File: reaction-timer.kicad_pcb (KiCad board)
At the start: 2 copper layers, 48 x 80 mm, 38 parts, among them IC1 4026, IC2 4026, IC3 4026, IC5 NE555P, IC6 NE555P, IC7 NE555P

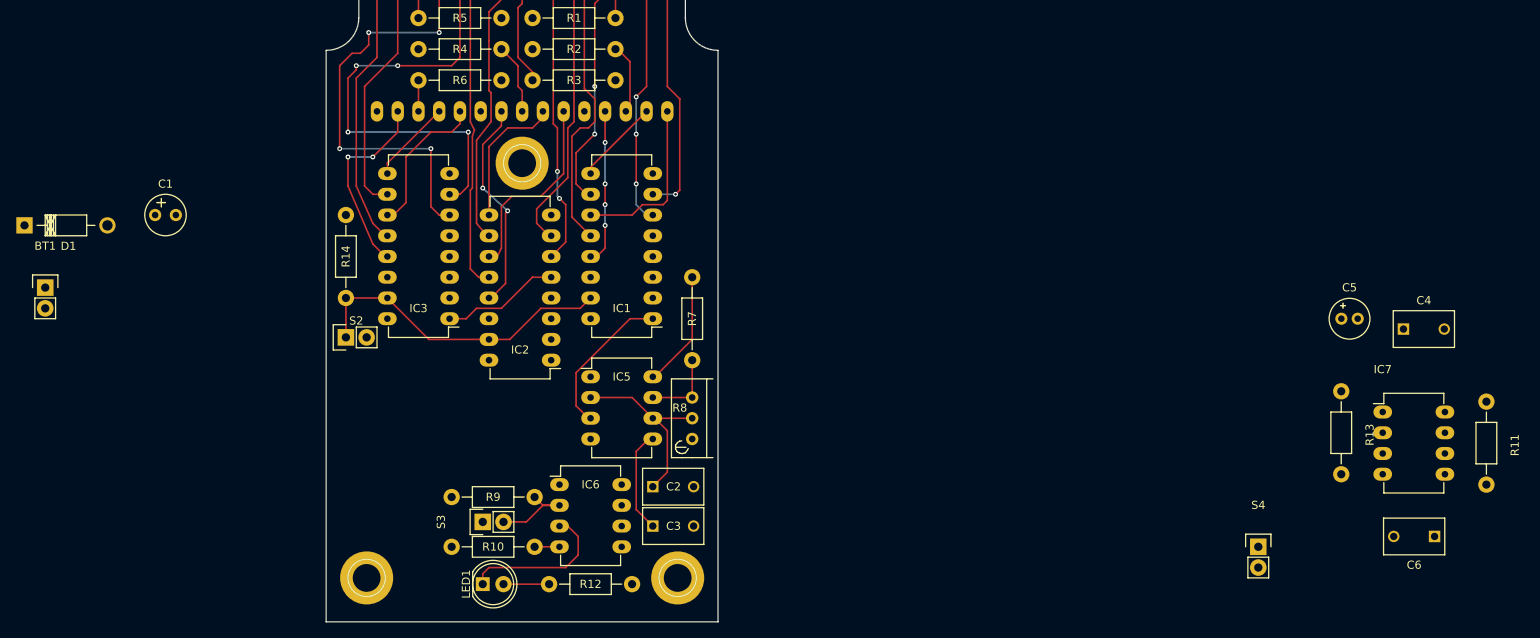
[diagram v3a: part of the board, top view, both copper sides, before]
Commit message: Place IC7
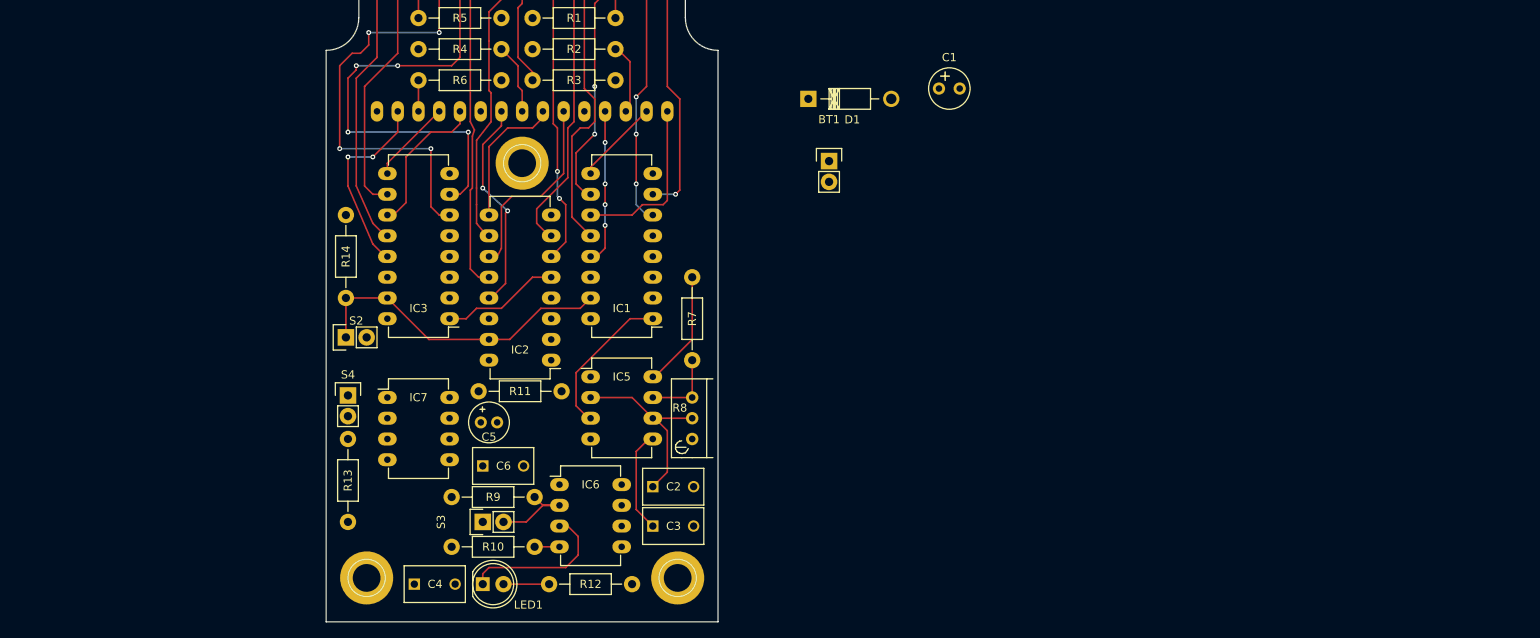
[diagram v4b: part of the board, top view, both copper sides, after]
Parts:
- moved C4 125.1 mm to (68.1, 136.7)
- moved IC7 121.9 mm to (64.8, 113.8)
- moved R13 121.8 mm to (59.9, 124.0)
- moved R11 118.5 mm to (81.0, 113.0), turned to 180 degrees
- moved C6 116.9 mm to (76.5, 122.2), turned to 0 degrees
- moved S4 113.0 mm to (59.9, 113.5)
- moved C5 106.2 mm to (76.2, 116.8)
- moved BT1 97.3 mm to (118.9, 84.8)
- moved C1 97.3 mm to (132.3, 75.9)
- moved D1 97.3 mm to (116.3, 77.2)
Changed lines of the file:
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@@
   )
   (module Pin_Headers:Pin_Header_Straight_1x02 (layer F.Cu)
-    (at 22.86 100.33)
+    (at 118.872 84.836)
     (descr "Through hole pin header")
     (tags "pin header")
@@
   )
   (module Capacitors_Elko_ThroughHole:Elko_vert_11x5mm_RM2.5 (layer F.Cu)
-    (at 36.322 91.44)
+    (at 132.334 75.946)
     (descr "Electrolytic Capacitor, vertical, diameter 5mm, radial, RM 2,5mm")
     (tags "Electrolytic Capacitor, vertical, diameter 5mm, radial, RM 2,5mm, Elko, Electrolytkondensator, Kondensator gepolt, Durchmesser 5mm")
@@
   )
   (module Capacitors_ThroughHole:C_Disc_D7.5_P5 (layer F.Cu)
-    (at 189.23 105.41)
+    (at 68.072 136.652)
     (descr "Capacitor 7.5mm Disc, Pitch 5mm")
     (tags Capacitor)
-    (fp_text reference C4 (at 2.5 -3.5) (layer F.SilkS)
+    (fp_text reference C4 (at 2.54 0) (layer F.SilkS)
       (effects (font (size 1 1) (thickness 0.15)))
     )
@@
   )
   (module Capacitors_Elko_ThroughHole:Elko_vert_11x5mm_RM2 (layer F.Cu)
-    (at 181.61 104.14)
+    (at 76.2 116.84)
     (descr "Electrolytic Capacitor, vertical, diameter 5mm, RM 2mm, radial,")
     (tags "Electrolytic Capacitor, vertical, diameter 5mm,  radial, RM 2mm, Elko, Electrolytkondensator, Kondensator gepolt, Durchmesser 5mm")
-    (fp_text reference C5 (at 1.016 -3.81) (layer F.SilkS)
+    (fp_text reference C5 (at 1.016 1.778) (layer F.SilkS)
       (effects (font (size 1 1) (thickness 0.15)))
     )
@@
   )
   (module Capacitors_ThroughHole:C_Disc_D7.5_P5 (layer F.Cu)
-    (at 193.04 130.81 180)
+    (at 76.454 122.174)
     (descr "Capacitor 7.5mm Disc, Pitch 5mm")
     (tags Capacitor)
-    (fp_text reference C6 (at 2.5 -3.5 180) (layer F.SilkS)
-      (effects (font (size 1 1) (thickness 0.15)))
-    )
-    (fp_text value C (at 2.5 3.5 180) (layer F.Fab)
+    (fp_text reference C6 (at 2.54 0) (layer F.SilkS)
+      (effects (font (size 1 1) (thickness 0.15)))
+    )
+    (fp_text value C (at 2.5 3.5) (layer F.Fab)
       (effects (font (size 1 1) (thickness 0.15)))
     )
@@
     (fp_line (start 6.25 2.25) (end -1.25 2.25) (layer F.SilkS) (width 0.15))
     (fp_line (start -1.25 2.25) (end -1.25 -2.25) (layer F.SilkS) (width 0.15))
-    (pad 1 thru_hole rect (at 0 0 180) (size 1.4 1.4) (drill 0.9) (layers *.Cu *.Mask F.SilkS)
+    (pad 1 thru_hole rect (at 0 0) (size 1.4 1.4) (drill 0.9) (layers *.Cu *.Mask F.SilkS)
       (net 39 "Net-(C6-Pad1)"))
-    (pad 2 thru_hole circle (at 5 0 180) (size 1.4 1.4) (drill 0.9) (layers *.Cu *.Mask F.SilkS)
+    (pad 2 thru_hole circle (at 5 0) (size 1.4 1.4) (drill 0.9) (layers *.Cu *.Mask F.SilkS)
       (net 32 GND))
     (model Capacitors_ThroughHole.3dshapes/C_Disc_D7.5_P5.wrl
@@
   )
   (module Diodes_ThroughHole:Diode_DO-41_SOD81_Horizontal_RM10 (layer F.Cu)
-    (at 20.32 92.71)
+    (at 116.332 77.216)
     (descr "Diode, DO-41, SOD81, Horizontal, RM 10mm,")
     (tags "Diode, DO-41, SOD81, Horizontal, RM 10mm, 1N4007, SB140,")
@@
   )
   (module Housings_DIP:DIP-8_W7.62mm_LongPads (layer F.Cu)
-    (at 186.69 115.57)
+    (at 64.77 113.792)
     (descr "8-lead dip package, row spacing 7.62 mm (300 mils), longer pads")
     (tags "dil dip 2.54 300")
-    (fp_text reference IC7 (at 0 -5.22) (layer F.SilkS)
+    (fp_text reference IC7 (at 3.81 0) (layer F.SilkS)
       (effects (font (size 1 1) (thickness 0.15)))
     )
@@
     (descr "LED vertical 5mm")
     (tags "LED-5MM LED 5mm")
-    (fp_text reference LED1 (at -2.032 0 90) (layer F.SilkS)
+    (fp_text reference LED1 (at 5.588 2.54 180) (layer F.SilkS)
       (effects (font (size 1 1) (thickness 0.15)))
     )
@@
   )
   (module Resistors_ThroughHole:Resistor_Horizontal_RM10mm (layer F.Cu)
-    (at 199.39 119.38 270)
+    (at 81.026 113.03 180)
     (descr "Resistor, Axial,  RM 10mm, 1/3W,")
     (tags "Resistor, Axial, RM 10mm, 1/3W,")
-    (fp_text reference R11 (at 0.24892 -3.50012 270) (layer F.SilkS)
-      (effects (font (size 1 1) (thickness 0.15)))
-    )
-    (fp_text value R (at 3.81 3.81 270) (layer F.Fab)
-      (effects (font (size 1 1) (thickness 0.15)))
-    )
-    (fp_line (start -2.54 -1.27) (end 2.54 -1.27) (layer F.SilkS) (width 0.15))
-    (fp_line (start 2.54 -1.27) (end 2.54 1.27) (layer F.SilkS) (width 0.15))
-    (fp_line (start 2.54 1.27) (end -2.54 1.27) (layer F.SilkS) (width 0.15))
-    (fp_line (start -2.54 1.27) (end -2.54 -1.27) (layer F.SilkS) (width 0.15))
-    (fp_line (start -2.54 0) (end -3.81 0) (layer F.SilkS) (width 0.15))
-    (fp_line (start 2.54 0) (end 3.81 0) (layer F.SilkS) (width 0.15))
-    (pad 1 thru_hole circle (at -5.08 0 270) (size 1.99898 1.99898) (drill 1.00076) (layers *.Cu *.SilkS *.Mask)
-      (net 33 "Net-(C1-Pad1)"))
-    (pad 2 thru_hole circle (at 5.08 0 270) (size 1.99898 1.99898) (drill 1.00076) (layers *.Cu *.SilkS *.Mask)
-      (net 38 "Net-(C5-Pad1)"))
-    (model Resistors_ThroughHole.3dshapes/Resistor_Horizontal_RM10mm.wrl
-      (at (xyz 0 0 0))
-      (scale (xyz 0.4 0.4 0.4))
-      (rotate (xyz 0 0 0))
-    )
-  )
-  (module Resistors_ThroughHole:Resistor_Horizontal_RM10mm (layer F.Cu)
-    (at 89.662 136.652 180)
-    (descr "Resistor, Axial,  RM 10mm, 1/3W,")
-    (tags "Resistor, Axial, RM 10mm, 1/3W,")
-    (fp_text reference R12 (at 0 0 180) (layer F.SilkS)
+    (fp_text reference R11 (at 0 0 180) (layer F.SilkS)
       (effects (font (size 1 1) (thickness 0.15)))
     )
@@
       (net 33 "Net-(C1-Pad1)"))
     (pad 2 thru_hole circle (at 5.08 0 180) (size 1.99898 1.99898) (drill 1.00076) (layers *.Cu *.SilkS *.Mask)
+      (net 38 "Net-(C5-Pad1)"))
+    (model Resistors_ThroughHole.3dshapes/Resistor_Horizontal_RM10mm.wrl
+      (at (xyz 0 0 0))
+      (scale (xyz 0.4 0.4 0.4))
+      (rotate (xyz 0 0 0))
+    )
+  )
+  (module Resistors_ThroughHole:Resistor_Horizontal_RM10mm (layer F.Cu)
+    (at 89.662 136.652 180)
+    (descr "Resistor, Axial,  RM 10mm, 1/3W,")
+    (tags "Resistor, Axial, RM 10mm, 1/3W,")
+    (fp_text reference R12 (at 0 0 180) (layer F.SilkS)
+      (effects (font (size 1 1) (thickness 0.15)))
+    )
+    (fp_text value R (at 3.81 3.81 180) (layer F.Fab)
+      (effects (font (size 1 1) (thickness 0.15)))
+    )
+    (fp_line (start -2.54 -1.27) (end 2.54 -1.27) (layer F.SilkS) (width 0.15))
+    (fp_line (start 2.54 -1.27) (end 2.54 1.27) (layer F.SilkS) (width 0.15))
+    (fp_line (start 2.54 1.27) (end -2.54 1.27) (layer F.SilkS) (width 0.15))
+    (fp_line (start -2.54 1.27) (end -2.54 -1.27) (layer F.SilkS) (width 0.15))
+    (fp_line (start -2.54 0) (end -3.81 0) (layer F.SilkS) (width 0.15))
+    (fp_line (start 2.54 0) (end 3.81 0) (layer F.SilkS) (width 0.15))
+    (pad 1 thru_hole circle (at -5.08 0 180) (size 1.99898 1.99898) (drill 1.00076) (layers *.Cu *.SilkS *.Mask)
+      (net 33 "Net-(C1-Pad1)"))
+    (pad 2 thru_hole circle (at 5.08 0 180) (size 1.99898 1.99898) (drill 1.00076) (layers *.Cu *.SilkS *.Mask)
       (net 50 "Net-(LED1-Pad2)"))
     (model Resistors_ThroughHole.3dshapes/Resistor_Horizontal_RM10mm.wrl
@@
   )
   (module Resistors_ThroughHole:Resistor_Horizontal_RM10mm (layer F.Cu)
-    (at 181.61 118.11 270)
+    (at 59.944 123.952 270)
     (descr "Resistor, Axial,  RM 10mm, 1/3W,")
     (tags "Resistor, Axial, RM 10mm, 1/3W,")
-    (fp_text reference R13 (at 0.24892 -3.50012 270) (layer F.SilkS)
+    (fp_text reference R13 (at 0 0 270) (layer F.SilkS)
       (effects (font (size 1 1) (thickness 0.15)))
     )
@@
   )
   (module Pin_Headers:Pin_Header_Straight_1x02 (layer F.Cu)
-    (at 171.45 132.08)
+    (at 59.944 113.538)
     (descr "Through hole pin header")
     (tags "pin header")
-    (fp_text reference S4 (at 0 -5.1) (layer F.SilkS)
+    (fp_text reference S4 (at 0 -2.54) (layer F.SilkS)
       (effects (font (size 1 1) (thickness 0.15)))
     )
@@
   (segment (start 85.852 127) (end 83.82 127) (width 0.2) (layer F.Cu) (net 46))
   (segment (start 83.82 127) (end 82.804 125.984) (width 0.2) (layer F.Cu) (net 46))
-  (segment (start 78.99266 136.652) (end 84.582 136.652) (width 0.2) (layer F.Cu) (net 50) (status C00000))
+  (segment (start 78.99266 136.652) (end 84.582 136.652) (width 0.2) (layer F.Cu) (net 50))
 )

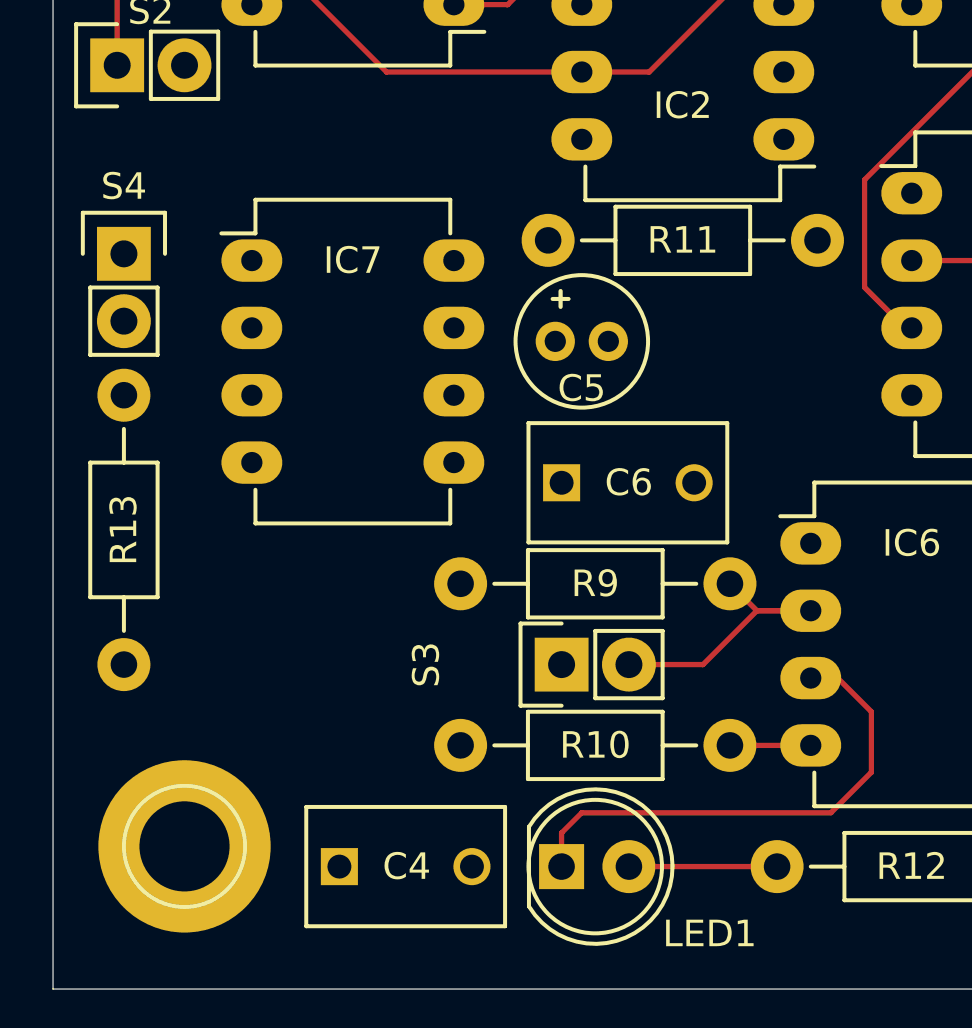
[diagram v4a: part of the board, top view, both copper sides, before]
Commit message: Connect IC7
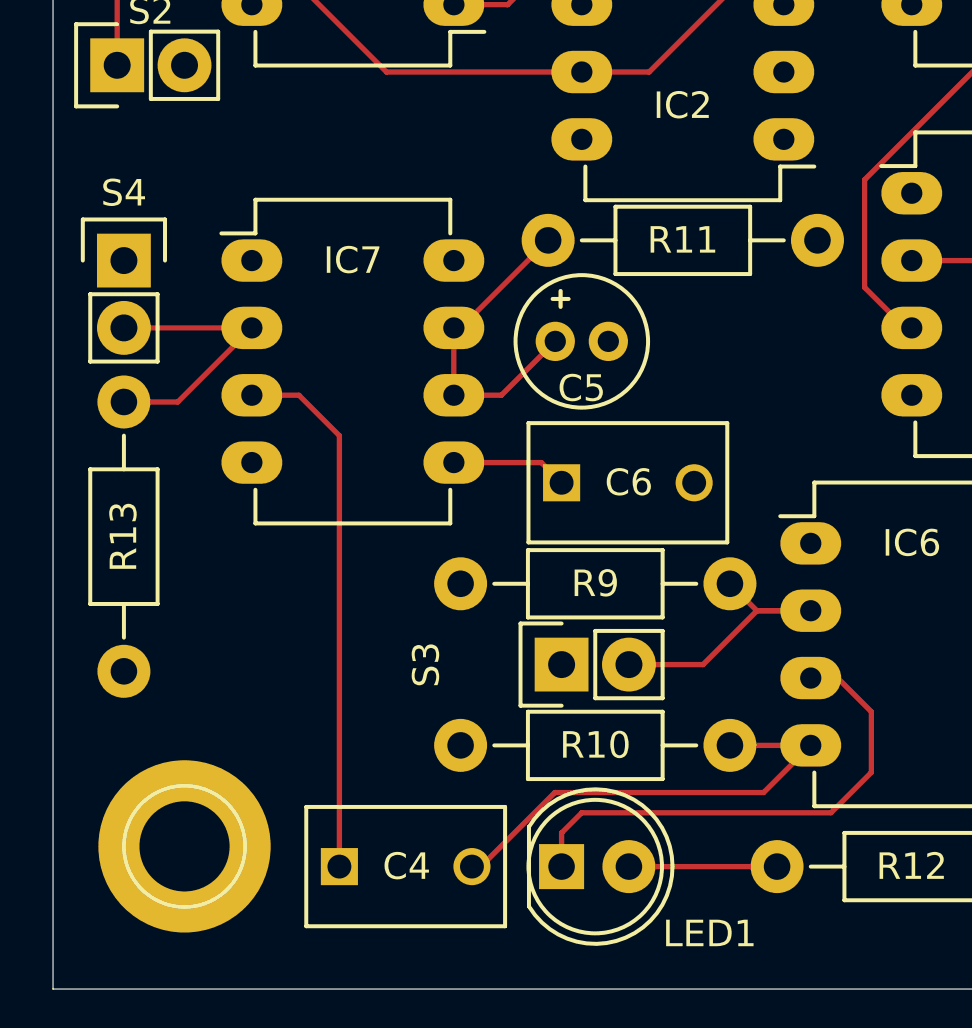
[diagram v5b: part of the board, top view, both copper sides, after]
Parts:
- moved R13 0.25 mm to (59.9, 124.2)
- moved S4 0.25 mm to (59.9, 113.8)
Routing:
- net Net-(C4-Pad1): track 0.00 -> 20.2 mm
- net Net-(C4-Pad2): track 3.05 -> 17.7 mm
- net Net-(C5-Pad1): track 0.00 -> 12.1 mm
- net Net-(IC7-Pad2): track 0.00 -> 10.8 mm
- net Net-(C6-Pad1): track 0.00 -> 4.38 mm
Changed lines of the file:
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@@
   (general
     (links 104)
-    (no_connects 59)
+    (no_connects 51)
     (area 17.504999 61.244999 204.617501 195.285)
     (thickness 1.6)
     (drawings 8)
-    (tracks 238)
+    (tracks 255)
     (zones 0)
     (modules 38)
@@
   )
   (module Resistors_ThroughHole:Resistor_Horizontal_RM10mm (layer F.Cu)
-    (at 59.944 123.952 270)
+    (at 59.944 124.206 270)
     (descr "Resistor, Axial,  RM 10mm, 1/3W,")
     (tags "Resistor, Axial, RM 10mm, 1/3W,")
@@
   )
   (module Pin_Headers:Pin_Header_Straight_1x02 (layer F.Cu)
-    (at 59.944 113.538)
+    (at 59.944 113.792)
     (descr "Through hole pin header")
     (tags "pin header")
@@
   (segment (start 95.25 120.396) (end 95.25 127.508) (width 0.2) (layer F.Cu) (net 35))
   (segment (start 95.25 127.508) (end 97.282 129.54) (width 0.2) (layer F.Cu) (net 35))
+  (segment (start 64.77 118.872) (end 66.548 118.872) (width 0.2) (layer F.Cu) (net 36) (status 400000))
+  (segment (start 68.072 120.396) (end 68.072 136.652) (width 0.2) (layer F.Cu) (net 36) (status 800000))
+  (segment (start 66.548 118.872) (end 68.072 120.396) (width 0.2) (layer F.Cu) (net 36))
+  (segment (start 73.072 136.652) (end 73.406 136.652) (width 0.2) (layer F.Cu) (net 37) (status C00000))
+  (segment (start 73.406 136.652) (end 76.2 133.858) (width 0.2) (layer F.Cu) (net 37) (status 400000))
+  (segment (start 76.2 133.858) (end 84.074 133.858) (width 0.2) (layer F.Cu) (net 37))
+  (segment (start 84.074 133.858) (end 85.852 132.08) (width 0.2) (layer F.Cu) (net 37) (status 800000))
   (segment (start 82.804 132.08) (end 85.852 132.08) (width 0.2) (layer F.Cu) (net 37))
+  (segment (start 72.39 116.332) (end 72.644 116.332) (width 0.2) (layer F.Cu) (net 38) (status C00000))
+  (segment (start 72.644 116.332) (end 75.946 113.03) (width 0.2) (layer F.Cu) (net 38) (status C00000))
+  (segment (start 72.39 118.872) (end 74.18324 118.872) (width 0.2) (layer F.Cu) (net 38) (status 400000))
+  (segment (start 74.18324 118.872) (end 76.21524 116.84) (width 0.2) (layer F.Cu) (net 38) (status 800000))
+  (segment (start 72.39 118.872) (end 72.39 116.332) (width 0.2) (layer F.Cu) (net 38) (status C00000))
+  (segment (start 72.39 121.412) (end 75.692 121.412) (width 0.2) (layer F.Cu) (net 39) (status 400000))
+  (segment (start 75.692 121.412) (end 76.454 122.174) (width 0.2) (layer F.Cu) (net 39) (status 800000))
   (segment (start 89.662 116.332) (end 89.408 116.332) (width 0.2) (layer F.Cu) (net 40))
   (segment (start 89.408 116.332) (end 87.884 114.808) (width 0.2) (layer F.Cu) (net 40))
@@
   (segment (start 85.852 127) (end 83.82 127) (width 0.2) (layer F.Cu) (net 46))
   (segment (start 83.82 127) (end 82.804 125.984) (width 0.2) (layer F.Cu) (net 46))
+  (segment (start 59.944 119.126) (end 61.976 119.126) (width 0.2) (layer F.Cu) (net 49) (status 400000))
+  (segment (start 61.976 119.126) (end 64.77 116.332) (width 0.2) (layer F.Cu) (net 49) (status 800000))
+  (segment (start 64.77 116.332) (end 59.944 116.332) (width 0.2) (layer F.Cu) (net 49) (status C00000))
   (segment (start 78.99266 136.652) (end 84.582 136.652) (width 0.2) (layer F.Cu) (net 50))
 )
